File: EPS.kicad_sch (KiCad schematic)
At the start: 13 parts, among them J2 PH1RA-02-UA, J3 WJ126V-5.0-2P, J4 USB_C_Receptacle_USB2.0_16P, J6 TagConnect_TC2030-NL

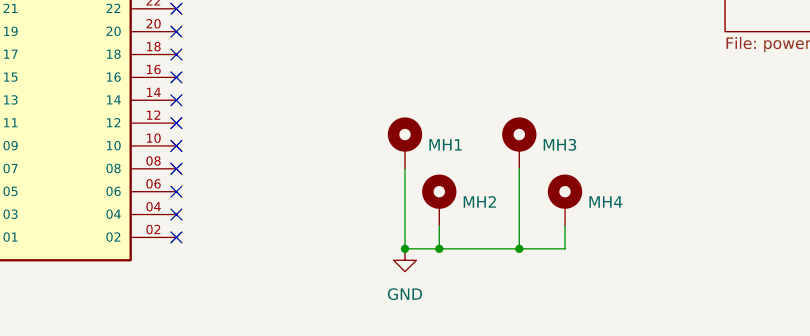
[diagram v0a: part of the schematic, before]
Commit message: Added most 3d models, continued layout
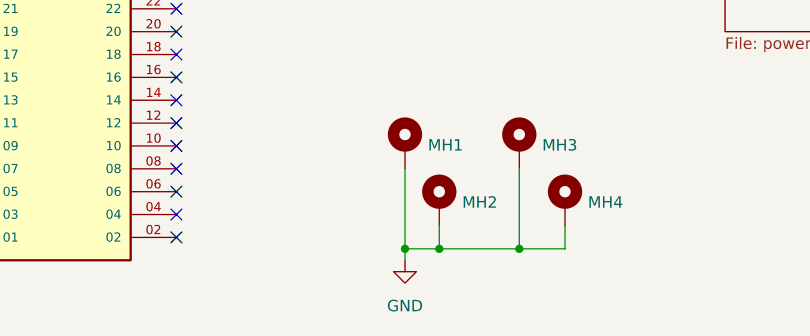
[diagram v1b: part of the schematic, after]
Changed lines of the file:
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@@
 	)
 	(junction
-		(at 184.15 60.96)
+		(at 92.71 179.07)
 		(diameter 0)
 		(color 0 0 0 0)
 	)
 	(junction
-		(at 137.16 36.83)
+		(at 184.15 60.96)
 		(diameter 0)
 		(color 0 0 0 0)
 	)
 	(junction
-		(at 209.55 34.29)
+		(at 137.16 36.83)
 		(diameter 0)
 		(color 0 0 0 0)
 	)
 	(junction
-		(at 105.41 179.07)
+		(at 209.55 34.29)
 		(diameter 0)
 		(color 0 0 0 0)
 	)
 	(junction
-		(at 92.71 179.07)
+		(at 105.41 179.07)
 		(diameter 0)
 		(color 0 0 0 0)
@@
 	(wire
 		(pts
+			(xy 92.71 179.07) (xy 92.71 180.34)
+		)
+		(stroke
+			(width 0)
+			(type default)
+		)
+	)
+	(wire
+		(pts
 			(xy 209.55 41.91) (xy 209.55 39.37)
 		)
@@
 	(symbol
 		(lib_id "power:GND")
-		(at 92.71 179.07 0)
+		(at 92.71 180.34 0)
 		(unit 1)
 		(exclude_from_sim no)
@@
 		(fields_autoplaced yes)
 		(property "Reference" "#PWR0105"
-			(at 92.71 185.42 0)
+			(at 92.71 186.69 0)
 			(effects
 				(font
@@
 		)
 		(property "Value" "GND"
-			(at 92.71 184.15 0)
+			(at 92.71 185.42 0)
 			(effects
 				(font
@@
 		)
 		(property "Footprint" ""
-			(at 92.71 179.07 0)
+			(at 92.71 180.34 0)
 			(effects
 				(font
@@
 		)
 		(property "Datasheet" ""
-			(at 92.71 179.07 0)
+			(at 92.71 180.34 0)
 			(effects
 				(font
@@
 		)
 		(property "Description" "Power symbol creates a global label with name \"GND\" , ground"
-			(at 92.71 179.07 0)
+			(at 92.71 180.34 0)
 			(effects
 				(font

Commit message: Rev 1 version
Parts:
- removed J3: WJ126V-5.0-2P, HEDGE2:WJ126V-5.0-2P, symbol HEDGE2:WJ126V-5.0-2P
- removed J4: USB_C_Receptacle_USB2.0_16P, Connector_USB:USB_C_Receptacle_HCTL_HC-TYPE-C-16P-01A, symbol Connector:USB_C_Receptacle_USB2.0_16P
- removed J6: TagConnect_TC2030-NL, Connector:Tag-Connect_TC2030-IDC-NL_2x03_P1.27mm_Vertical, symbol Connector:Conn_ARM_SWD_TagConnect_TC2030-NL
- removed R70, R71: 5k1, Resistor_SMD:R_0402_1005Metric, symbol Device:R_Small
- removed R72: 4k7, Resistor_SMD:R_0402_1005Metric, symbol Device:R_Small
- added A1: RaspberryPi_Pico, Module:RaspberryPi_Pico_SMD_HandSolder, symbol MCU_Module:RaspberryPi_Pico_Debug
- added BT1, BT2, BT3: 1043, HEDGE2-EPS:BAT_1043, symbol HEDGE2:1043
- added C1, C12, C13, C14, C15, C17, C19, C21, C23, C24, C25, C26, C27, C28, C29, C34, C6, C7, C8, C9: 100n, Capacitor_SMD:C_0603_1608Metric, symbol Device:C_Small
- added C10, C11: 22u, Capacitor_SMD:C_1206_3216Metric, symbol Device:C_Small
- added C16, C18, C20, C22: 1n, Capacitor_SMD:C_0603_1608Metric, symbol Device:C_Small
- added C2, C3, C4, C5: 47u, Capacitor_SMD:C_1206_3216Metric, symbol Device:C_Small
- added C30, C31, C32, C33: 10p, Capacitor_SMD:C_0603_1608Metric, symbol Device:C_Small
- added C35: 10uF, Capacitor_SMD:C_0603_1608Metric, symbol Device:C_Small
- added D1: Zener, Diode_SMD:D_SOD-123, symbol Device:D_Zener_Small
- added D2: Schottky, Diode_SMD:D_SOD-123, symbol Device:D_Schottky_Small
- added D3, D4: LED, LED_SMD:LED_0603_1608Metric, symbol Device:LED
- added D9: SM712-02HTG, HEDGE2-EPS:SM71202HTG, symbol HEDGE2:SM712-02HTG
- added IC1, IC3, IC7, IC8: TPS22997RYZR, HEDGE2-EPS:TPS22997RYZR, symbol HEDGE2:TPS22997RYZR
- added IC10: SN65HVD1782QDRQ1, HEDGE2-EPS:SN65HVD1782QDRQ1, symbol HEDGE2:SN65HVD1782QDRQ1
- added IC11, IC12: MCP2518FDT-E_SL, HEDGE2-EPS:MCP2518FDT-E_SL, symbol HEDGE2:MCP2518FDT-E_SL
- added IC2: TPS56C230RJER, HEDGE2-EPS:TPS56C230RJER, symbol HEDGE2:TPS56C230RJER
- added IC9: TCAN1046AVDYYRQ1, HEDGE2-EPS:TCAN1046AVDYYRQ1, symbol HEDGE2:TCAN1046AVDYYRQ1
- added J1: S4B-XH-A_LF__SN_, HEDGE2-EPS:S4BXHALFSN, symbol HEDGE2:S4B-XH-A_LF__SN_
- added L1: 3u3, HEDGE2-EPS:744393465033, symbol Device:L_Small
- added Q1: SI4497DY-T1-GE3, HEDGE2-EPS:SI4497DY-T1-GE3, symbol HEDGE2:SI4497DY-T1-GE3
- added R1: 100k, Resistor_SMD:R_0603_1608Metric, symbol Device:R_Small_US
- added R10, R11, R9: 4k7, Resistor_SMD:R_0603_1608Metric, symbol Device:R_Small_US
- added R12: 2k2, Resistor_SMD:R_0603_1608Metric, symbol Device:R_Small_US
- added R16, R17, R18, R19: 60, Resistor_SMD:R_0603_1608Metric, symbol Device:R_Small_US
- added R2: 110k, Resistor_SMD:R_0603_1608Metric, symbol Device:R_Small_US
- added R20, R21, R8: 10k, Resistor_SMD:R_0603_1608Metric, symbol Device:R_Small_US
- added R22, R23: 10, Resistor_SMD:R_0603_1608Metric, symbol Device:R_Small_US
- added R3: 15k, Resistor_SMD:R_0603_1608Metric, symbol Device:R_Small_US
- added R4: 180k, Resistor_SMD:R_0603_1608Metric, symbol Device:R_Small_US
- added R5: 33k, Resistor_SMD:R_0603_1608Metric, symbol Device:R_Small_US
- added R6: 205k, Resistor_SMD:R_0603_1608Metric, symbol Device:R_Small_US
- added R7: 51k1, Resistor_SMD:R_0603_1608Metric, symbol Device:R_Small_US
- added U1, U2, U3, U4, U5: INA260, Package_SO:TSSOP-16_4.4x5mm_P0.65mm, symbol Sensor:INA260
- added Y1, Y2: 40MHz, HEDGE2-EPS:ABM10AIG-40.000MHZ-7-J1Z-T, symbol Device:Crystal_GND24_Small
- H1EPS1, H2EPS1: footprint HEDGE2:SAMTEC_ESQ-126-39-G-D -> HEDGE2-EPS:SAMTEC_ESQ-126-39-G-D
- J2: footprint HEDGE2:PH1RA02UA -> HEDGE2-EPS:PH1RA02UA
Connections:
- net CHARGE is gone; now on net BATT: H2EPS1.43, H2EPS1.44
- net BATT: now also H2EPS1.41, H2EPS1.42, Q1.1 (S_1), Q1.2 (S_2), Q1.3 (S_3), U3.1 (IN+), U3.12 (VBUS), U3.2 (IN+), U3.3 (IN+)
- net CAN_A_H: now also IC9.13 (CANH1), R16.1
- net CAN_A_L: now also IC9.12 (CANL1), R17.2
- net CAN_B_H: now also IC9.10 (CANH2), R18.1
- net CAN_B_L: now also IC9.9 (CANL2), R19.2
- net GND: now also H1EPS1.33, H1EPS1.34, A1.13 (GND), A1.18 (GND), A1.23 (GND), A1.28 (GND), A1.3 (GND), A1.33 (AGND), A1.38 (GND), A1.8 (GND), A1.D2 (GND), BT1.N, C10.2, C11.2, C12.2, C13.2, C14.2, C15.2, C16.2, C17.2, C18.2, C19.2, C2.2, C20.2, C21.2, C22.2, C23.2, C24.2, C25.2, C26.2, C27.2, C28.2, C29.2, C3.2, C30.2, C31.2, C32.2, C33.2, C34.2, C35.2, C4.2, C5.2, C6.2, C7.2, C8.2, C9.2, D1.2 (A), D9.3, IC1.5 (GND), IC10.5 (GND), IC11.7 (VSS), IC12.7 (VSS), IC2.10 (NC_1), IC2.13 (AGND), IC2.16 (NC_2), IC2.18 (PGND_3), IC2.21 (PGND_4), IC2.7 (PGND_1), IC2.8 (PGND_2), IC3.5 (GND), IC7.5 (GND), IC8.5 (GND), IC9.14 (STB1), IC9.2 (GND1), IC9.5 (GND2), IC9.8 (STB2), J1.1, R11.2, R12.2, R21.2, R3.2, R5.2, R7.2, R8.1, U1.11 (GND), U1.4 (A1), U1.6 (GND), U2.11 (GND), U2.4 (A1), U2.6 (GND), U3.11 (GND), U3.4 (A1), U3.5 (A0), U3.6 (GND), U4.11 (GND), U4.4 (A1), U4.6 (GND), U5.11 (GND), U5.5 (A0), U5.6 (GND), Y1.2, Y1.4, Y2.2, Y2.4; no longer H1EPS1.29, H1EPS1.30, H1EPS1.31, H1EPS1.32
- net DIN/CONFIG/DIO14_XB: now reaches H2EPS1.01
- net DOUT/DIO13_XB: now reaches H2EPS1.02
- net RTS/DIO6_XB: now reaches H2EPS1.03
- net CTS/DIO7_XB: now reaches H2EPS1.04
- net AD3/DIO3/SPI_SSEL_XB: now reaches H2EPS1.05
- net AD/DIO2/SPI_CLK_XB: now reaches H2EPS1.06
- net DIO4/SPI_MOSI_XB: now reaches H2EPS1.07
- net DIO12/SPI_MISO_XB: now reaches H2EPS1.08
- net DTR/SLEEP_RQ/DIO8_XB: now reaches H2EPS1.09
- net AD1/DIO1/SPI_ATTN_XB: now reaches H2EPS1.10
- net ON_SLEEP/DIO9_XB: now reaches H2EPS1.11
- net DIO10/PWM0_XB: now reaches H2EPS1.12
- net RESET_XB: now reaches H2EPS1.13
- net DIO11/PWM1_XB: now reaches H2EPS1.14
- net AD0/DIO0_XB: now reaches H2EPS1.15
- net Associate/DIO5_XB: now reaches H2EPS1.16
- net NDTR_XB: now reaches H2EPS1.17
- net MIC_IN_DMR: now reaches H2EPS1.19
- net LINE_OUT_DMR: now reaches H2EPS1.20
- net T/R_DMR: now reaches H2EPS1.21
- net PTT_DMR: now reaches H2EPS1.22
- net SPKEN_DMR: now reaches H2EPS1.23
- net CS_DMR: now reaches H2EPS1.24
- net HST_TXD_DMR: now reaches H2EPS1.27
- net UART_TX_DMR: now reaches H2EPS1.28
- net UART_G_TX (EPS): now reaches H1EPS1.41
- net UART_G_TX (EPS): now also D9.2, R22.2
- net UART_G_RX (EPS): now reaches H1EPS1.43
- net UART_G_RX (EPS): now also D9.1, R23.2
- removed net 5V_PERM: H1EPS1.25, H1EPS1.26, H2EPS1.25, H2EPS1.26
- net DS_A: no longer names the net of H2EPS1.48
- net DS_B: no longer names the net of H2EPS1.50
- net DS_C: no longer names the net of H2EPS1.52
- net ENA_PWR_1: no longer names the net of H1EPS1.45
- net ENA_PWR_2: no longer names the net of H1EPS1.47
- net ENA_PWR_3: no longer names the net of H1EPS1.49
- net ENA_PWR_4: no longer names the net of H1EPS1.51
- net ENA_PWR_5: no longer names the net of H2EPS1.33
- net ENA_PWR_6: no longer names the net of H2EPS1.35
- net ENA_PWR_7: no longer names the net of H2EPS1.37
- net ENA_PWR_8: no longer names the net of H2EPS1.39
- net PWR_1 renamed +5V_OBC
- net +5V_OBC: now also IC1.6 (QOD), IC1.7 (VOUT_1), IC1.8 (VOUT_2)
- net PWR_2 renamed +5V_GNSS
- net +5V_GNSS: now also IC8.6 (QOD), IC8.7 (VOUT_1), IC8.8 (VOUT_2)
- net PWR_3 renamed +5V_SCI
- net +5V_SCI: now also IC3.6 (QOD), IC3.7 (VOUT_1), IC3.8 (VOUT_2)
- net PWR_4 renamed +5V_COMM
- net +5V_COMM: now also IC7.6 (QOD), IC7.7 (VOUT_1), IC7.8 (VOUT_2)
- net PWR_5: no longer names the net of H2EPS1.34
- net PWR_6: no longer names the net of H2EPS1.36
- net PWR_7: no longer names the net of H2EPS1.38
- net PWR_8: no longer names the net of H2EPS1.40
- net RBF_A: no longer names the net of H2EPS1.47
- net RBF_B: no longer names the net of H2EPS1.49
- net RBF_C: no longer names the net of H2EPS1.51
- net RBF_INHIBIT renamed EN
- net EN: now also D1.1 (K), IC2.12 (EN), R6.2, R7.1
- net UART_A_RX: no longer names the net of H1EPS1.07
- net UART_A_TX: no longer names the net of H1EPS1.05
- net UART_B_RX: no longer names the net of H1EPS1.08
- net UART_B_TX: no longer names the net of H1EPS1.06
- net UART_C_RX: no longer names the net of H1EPS1.15
- net UART_C_TX: no longer names the net of H1EPS1.13
- net UART_D_RX: no longer names the net of H1EPS1.24
- net UART_D_TX: no longer names the net of H1EPS1.22
- net UART_E_RX renamed UART_E_RX (SCI)
- net UART_E_TX renamed UART_E_TX (SCI)
- net UART_F_RX renamed UART_F_RX (GNSS_RXD1)
- net UART_F_TX renamed UART_F_TX (GNSS_TXD1)
- new net: C16.1, IC1.9 (CT)
- new net: C30.1, IC11.6 (OSC1), Y1.3
- new net: D4.1 (K), R11.1
- new net: C20.1, IC7.9 (CT)
- new net: C26.1, R16.2, R17.1
- new net: C31.1, IC11.5 (OSC2), Y1.1
- new net: IC10.6 (A), R23.1
- new net: IC10.7 (B), R22.1
- new net: A1.39 (VSYS), D2.1 (K)
- new net: C18.1, IC3.9 (CT)
- new net: C22.1, IC8.9 (CT)
- new net: IC2.14 (FB), R2.2, R3.1
- new net: IC2.9 (PGOOD), R1.1
- new net: C6.1, IC2.17 (VCC), R1.2, R4.1
- new net: C28.1, R18.2, R19.1
- new net: C32.1, IC12.5 (OSC2), Y2.1
- new net: C33.1, IC12.6 (OSC1), Y2.3
- new net: C1.2, IC2.19 (SW_2), IC2.20 (SW_3), IC2.6 (SW_1), L1.1
- new net: D3.1 (K), R12.1
- new net: Q1.4 (G), R8.2
- new net: C1.1, IC2.1 (BST)
- new net: IC2.15 (MODE), R4.2, R5.1
- new net +3V3: A1.36 (3V3), C12.1, C13.1, C14.1, C23.1, C24.1, C27.1, C29.1, C34.1, C8.1, C9.1, IC10.8 (VCC), IC11.14 (VDD), IC12.14 (VDD), IC9.11 (VIO), R10.1, R20.1, R9.1, U1.10 (VS), U1.5 (A0), U2.10 (VS), U3.10 (VS), U4.10 (VS), U5.10 (VS), U5.4 (A1)
- new net +5V: C2.1, C25.1, C3.1, C35.1, C4.1, C5.1, D2.2 (A), D3.2 (A), IC9.3 (VCC), L1.2, R2.1, U1.1 (IN+), U1.12 (VBUS), U1.2 (IN+), U1.3 (IN+), U2.1 (IN+), U2.12 (VBUS), U2.2 (IN+), U2.3 (IN+), U4.1 (IN+), U4.12 (VBUS), U4.2 (IN+), U4.3 (IN+), U5.1 (IN+), U5.12 (VBUS), U5.2 (IN+), U5.3 (IN+)
- new net +5V_COMM_SENSE: C19.1, IC7.1 (VBIAS), IC7.2 (VIN_1), IC7.3 (VIN_2), U5.14 (IN-), U5.15 (IN-), U5.16 (IN-)
- new net +5V_GNSS_SENSE: C21.1, IC8.1 (VBIAS), IC8.2 (VIN_1), IC8.3 (VIN_2), U4.14 (IN-), U4.15 (IN-), U4.16 (IN-)
- new net +5V_OBC_SENSE: C15.1, IC1.1 (VBIAS), IC1.2 (VIN_1), IC1.3 (VIN_2), U1.14 (IN-), U1.15 (IN-), U1.16 (IN-)
- new net +5V_SCI_SENSE: C17.1, IC3.1 (VBIAS), IC3.2 (VIN_1), IC3.3 (VIN_2), U2.14 (IN-), U2.15 (IN-), U2.16 (IN-)
- new net +BATT_NP: BT3.P, J1.4, Q1.5 (D_1), Q1.6 (D_2), Q1.7 (D_3), Q1.8 (D_4)
- new net +BATT_SENSE: C10.1, C11.1, C7.1, D4.2 (A), IC2.2 (VIN_1), IC2.3 (VIN_2), IC2.4 (VIN_3), IC2.5 (VIN_4), R6.1, U3.14 (IN-), U3.15 (IN-), U3.16 (IN-)
- new net CAN_A_CS: A1.27 (GPIO21), IC11.13 (NCS)
- new net CAN_A_INT: A1.29 (GPIO22), IC11.4 (~{INT})
- new net CAN_B_CS: A1.22 (GPIO17), IC12.13 (NCS)
- new net CAN_B_INT: A1.26 (GPIO20), IC12.4 (~{INT})
- new net COMM_C: A1.20 (GPIO15), IC7.10 (ON)
- new net GNSS_C: A1.17 (GPIO13), IC8.10 (ON)
- new net HST_RXD_DMR: H2EPS1.25
- new net MISO: A1.21 (GPIO16), IC11.12 (SDO), IC12.12 (SDO)
- new net MOSI: A1.25 (GPIO19), IC11.11 (SDI), IC12.11 (SDI)
- new net OBC_C: A1.16 (GPIO12), IC1.10 (ON)
- new net RS485_E: A1.10 (GPIO7), IC10.2 (RE), IC10.3 (DE), R21.1
- new net RS485_RX: A1.12 (GPIO9), IC10.1 (R), R20.2
- new net RS485_TX: A1.11 (GPIO8), IC10.4 (D)
- new net RXCAN_A: IC11.2 (RXCAN), IC9.4 (RXD1)
- new net RXCAN_B: IC12.2 (RXCAN), IC9.7 (RXD2)
- new net SCI_C: A1.19 (GPIO14), IC3.10 (ON)
- new net SCK: A1.24 (GPIO18), IC11.10 (SCK), IC12.10 (SCK)
- new net SCL: A1.7 (GPIO5), R9.2, U1.9 (SCL), U2.5 (A0), U2.9 (SCL), U3.9 (SCL), U4.9 (SCL), U5.9 (SCL)
- new net SDA: A1.6 (GPIO4), R10.2, U1.8 (SDA), U2.8 (SDA), U3.8 (SDA), U4.5 (A0), U4.8 (SDA), U5.8 (SDA)
- new net TXCAN_A: IC11.1 (TXCAN), IC9.1 (TXD1)
- new net TXCAN_B: IC12.1 (TXCAN), IC9.6 (TXD2)
- new net UART_RX_DMR: H2EPS1.26
- new net VC1: BT1.P, BT2.N, J1.2
- new net VC2: BT2.P, BT3.N, J1.3
- no-connect marks 92 -> 86
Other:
- removed sheet Batteries
- removed sheet Control
- removed sheet Power Conversion
- removed sheet Power Input
- removed sheet Power Output
- note added: "2 Separation Switches?"
- note added: "5V Load Switches"
- note added: "5V Step Down Converter"
- note added: "Battery"
- note added: "Battery Inhibit"
- note added: "CANBUS Communication"
- note added: "Interboard Connectors"
- note added: "Microcontroller"
- note added: "Mounting Holes"
- note added: "Power Monitors"
- note added: "RS485 Communication"
- note added: "Status Indication"
- moved on the sheet: H1EPS1, H2EPS1, MH1, MH2, MH3, MH4

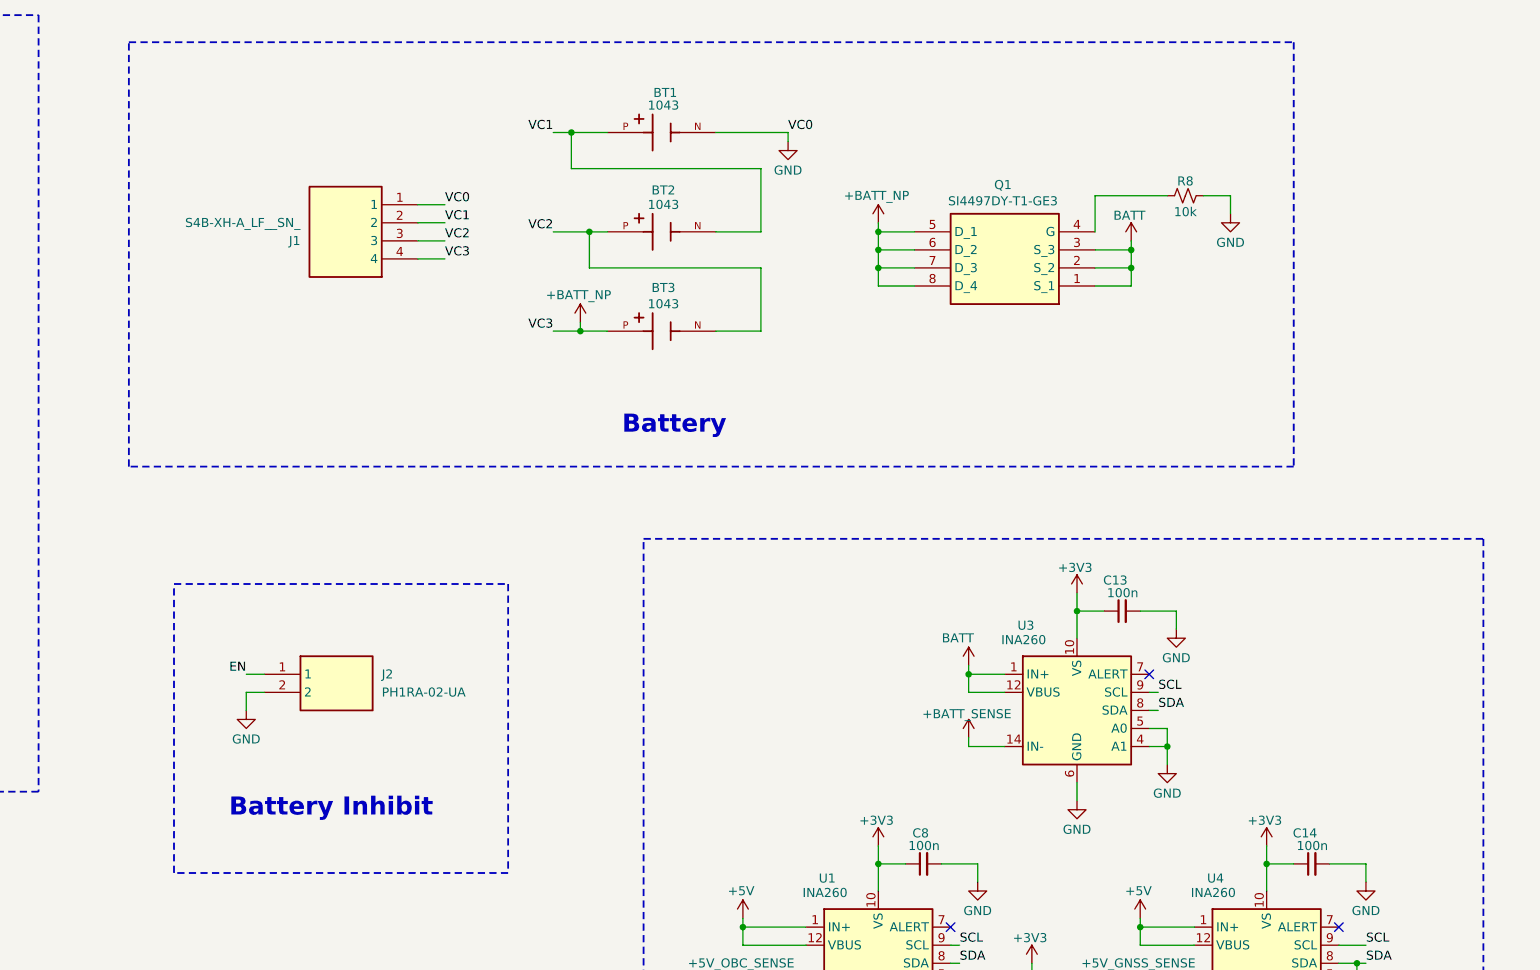
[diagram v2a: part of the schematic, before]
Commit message: Added sep switch connector and fixes
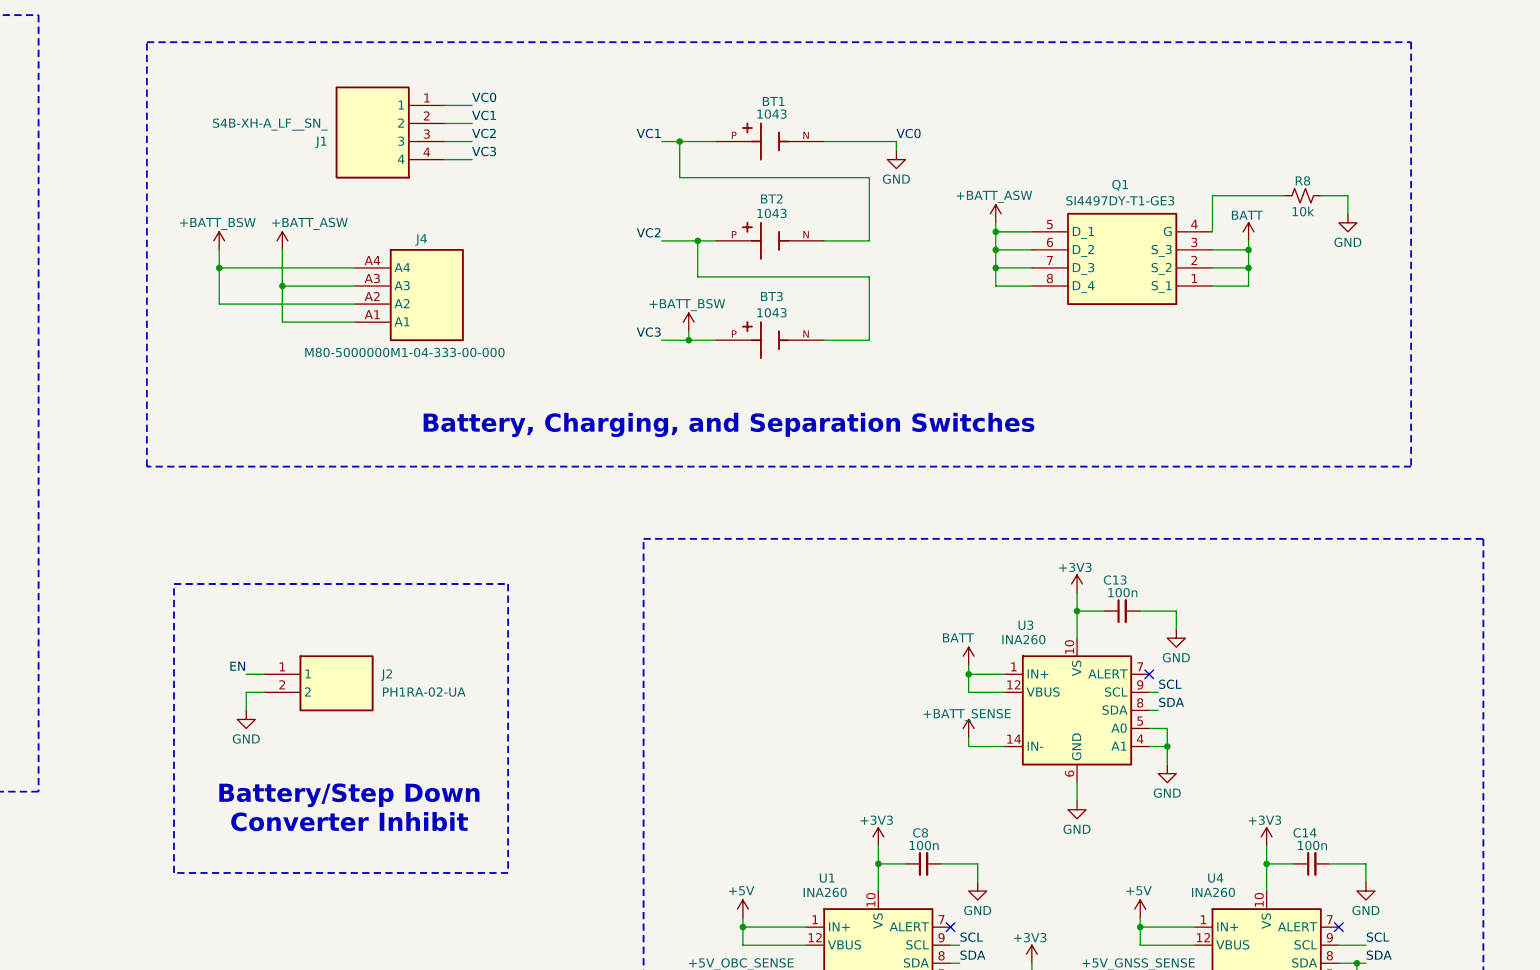
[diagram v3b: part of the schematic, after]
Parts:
- added J4: M80-5000000M1-04-333-00-000, M805000000M10433300000, symbol HEDGE2:M80-5000000M1-04-333-00-000
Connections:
- net +BATT_NP renamed +BATT_ASW
- net +BATT_ASW: now also J4.A1, J4.A3; no longer BT3.P, J1.4
- new net +BATT_BSW: BT3.P, J1.4, J4.A2, J4.A4
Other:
- note added: "Battery, Charging, and Separation Switches"
- note added: "Battery/Step Down Converter Inhibit"
- note removed: "Battery"
- note removed: "Battery Inhibit"
- moved on the sheet: BT1, BT2, BT3, J1, Q1, R8

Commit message: Fixed the rest of DRC errors
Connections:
- no-connect marks 86 -> 85
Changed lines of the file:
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@@
 	)
 	(no_connect
-		(at 502.92 57.15)
-	)
-	(no_connect
 		(at 92.71 180.34)
 	)
@@
 		(on_board yes)
 		(dnp no)
-		(fields_autoplaced yes)
 		(property "Reference" "J1"
-			(at 184.15 44.4501 0)
+			(at 183.134 39.624 0)
 			(effects
 				(font

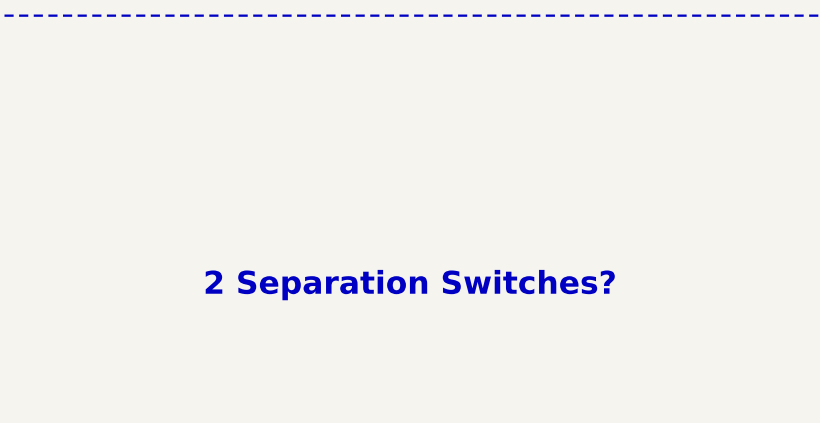
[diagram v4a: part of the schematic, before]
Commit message: cleaned up schematic
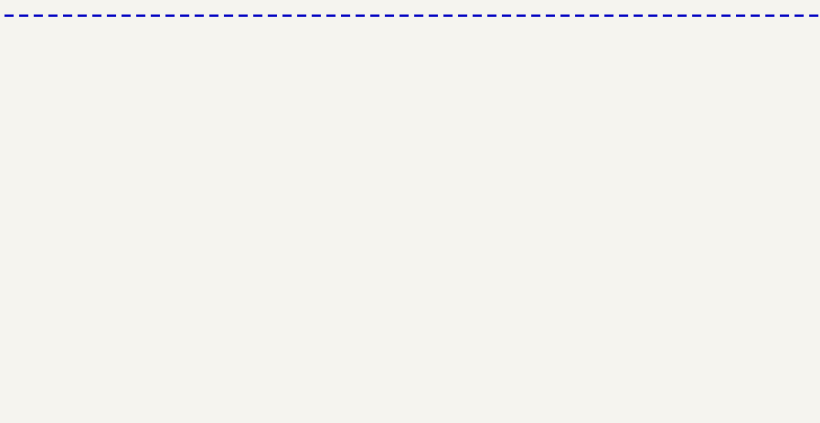
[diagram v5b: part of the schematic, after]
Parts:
- J4: footprint M805000000M10433300000 -> HEDGE2-EPS:M805000000M10433300000
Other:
- note removed: "2 Separation Switches?"
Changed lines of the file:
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@@
 		)
 	)
-	(text "2 Separation Switches?"
-		(exclude_from_sim no)
-		(at 268.732 369.062 0)
-		(effects
-			(font
-				(size 2.54 2.54)
-				(thickness 0.508)
-				(bold yes)
-			)
-		)
-	)
 	(text "RS485 Communication\n"
 		(exclude_from_sim no)
@@
 			)
 		)
-		(property "Footprint" "M805000000M10433300000"
+		(property "Footprint" "HEDGE2-EPS:M805000000M10433300000"
 			(at 204.47 157.15 0)
 			(effects

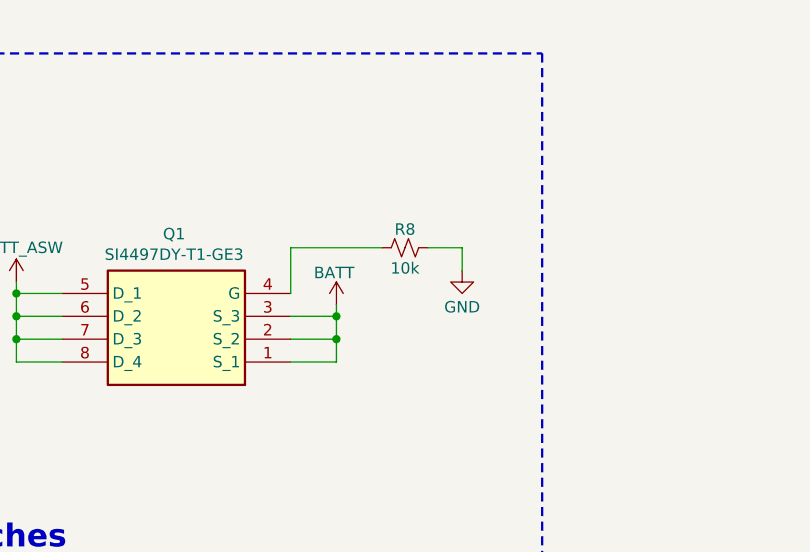
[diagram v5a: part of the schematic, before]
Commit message: Updated resistor val for reverse pol mosfet
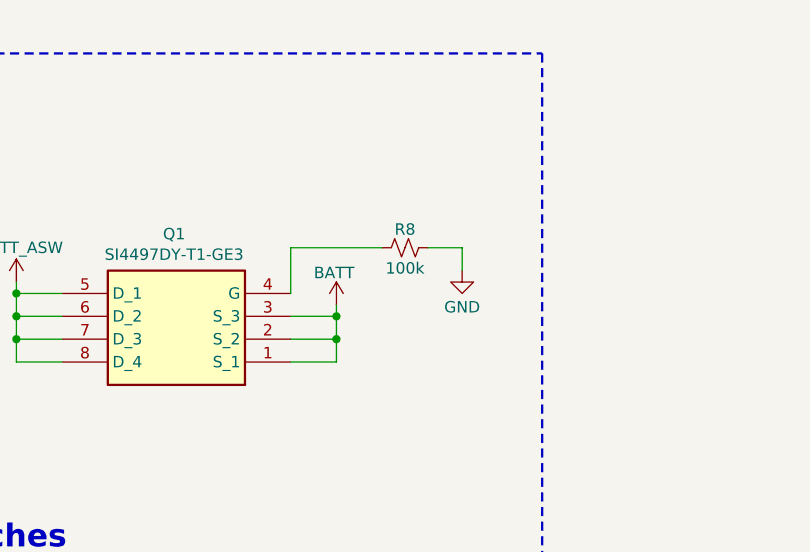
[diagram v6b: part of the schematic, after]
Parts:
- R8: value 10k -> 100k
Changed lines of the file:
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@@
 			)
 		)
-		(property "Value" "10k"
+		(property "Value" "100k"
 			(at 321.31 54.356 90)
 			(effects
